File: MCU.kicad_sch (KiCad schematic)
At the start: 33 parts, among them J7 RS485, J8 JTAG, J9 USB-C, SW1 SYS_RESET, SW2 BOOT0, U10 LTC2851xS8, U11 USBLC6-2SC6, U9 STM32G474MBTx, Y1 16MHz

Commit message: reorg and add 10MHz
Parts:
- removed TP7: VBUS, TestPoint:TestPoint_Keystone_5015_Micro_Mini, symbol Connector:TestPoint_Small
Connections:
- net +3.3V: now also U10.1 (VCC)
- net GND: now also U10.4 (GND)
- net VBUS: now reaches J9.A4 (VBUS), J9.A9 (VBUS), J9.B4 (VBUS), J9.B9 (VBUS)
- net EN_RF4: now reaches U9.36 (PE13)
- net PG_RF4: now reaches U9.37 (PE14)
- net BUCK_VIN renamed BUCKIN_SENSE
- net BUCK_VOUT renamed BUCKOUT_SENSE
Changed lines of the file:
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@@
 	(wire
 		(pts
+			(xy 176.53 92.71) (xy 176.53 99.06)
+		)
+		(stroke
+			(width 0)
+			(type default)
+		)
+	)
+	(wire
+		(pts
 			(xy 69.85 146.05) (xy 72.39 146.05)
 		)
@@
 	(wire
 		(pts
-			(xy 114.3 41.91) (xy 124.46 41.91)
+			(xy 114.3 41.91) (xy 130.81 41.91)
 		)
 		(stroke
@@
 	(wire
 		(pts
+			(xy 121.92 44.45) (xy 130.81 44.45)
+		)
+		(stroke
+			(width 0)
+			(type default)
+		)
+	)
+	(wire
+		(pts
 			(xy 114.3 24.13) (xy 121.92 24.13)
 		)
@@
 	(wire
 		(pts
+			(xy 44.45 69.85) (xy 49.53 69.85)
+		)
+		(stroke
+			(width 0)
+			(type default)
+		)
+	)
+	(wire
+		(pts
 			(xy 44.45 125.73) (xy 49.53 125.73)
 		)
@@
 	(wire
 		(pts
-			(xy 99.06 36.83) (xy 124.46 36.83)
+			(xy 99.06 36.83) (xy 130.81 36.83)
 		)
 		(stroke
@@
 	(wire
 		(pts
-			(xy 121.92 31.75) (xy 121.92 44.45)
-		)
-		(stroke
-			(width 0)
-			(type default)
-		)
-	)
-	(wire
-		(pts
 			(xy 34.29 44.45) (xy 44.45 44.45)
 		)
@@
 	(wire
 		(pts
+			(xy 176.53 54.61) (xy 176.53 62.23)
+		)
+		(stroke
+			(width 0)
+			(type default)
+		)
+	)
+	(wire
+		(pts
 			(xy 44.45 41.91) (xy 49.53 41.91)
 		)
@@
 	(wire
 		(pts
-			(xy 121.92 44.45) (xy 124.46 44.45)
+			(xy 234.95 113.03) (xy 234.95 115.57)
 		)
 		(stroke
@@
 	(wire
 		(pts
+			(xy 121.92 31.75) (xy 121.92 44.45)
+		)
+		(stroke
+			(width 0)
+			(type default)
+		)
+	)
+	(wire
+		(pts
 			(xy 214.63 92.71) (xy 214.63 95.25)
 		)
@@
 	(wire
 		(pts
+			(xy 44.45 72.39) (xy 49.53 72.39)
+		)
+		(stroke
+			(width 0)
+			(type default)
+		)
+	)
+	(wire
+		(pts
 			(xy 22.86 17.78) (xy 22.86 20.32)
 		)
@@
 	(wire
 		(pts
-			(xy 106.68 39.37) (xy 124.46 39.37)
+			(xy 106.68 39.37) (xy 130.81 39.37)
 		)
 		(stroke
@@
 		)
 	)
-	(hierarchical_label "BUCK_VOUT"
+	(hierarchical_label "BUCKOUT_SENSE"
 		(shape input)
-		(at 124.46 44.45 0)
+		(at 130.81 44.45 0)
 		(effects
 			(font
@@
 	(hierarchical_label "RFVA"
 		(shape input)
-		(at 124.46 36.83 0)
+		(at 130.81 36.83 0)
 		(effects
 			(font
@@
 		)
 	)
+	(hierarchical_label "EN_RF4"
+		(shape input)
+		(at 44.45 69.85 180)
+		(effects
+			(font
+				(size 1.27 1.27)
+			)
+			(justify right)
+		)
+	)
 	(hierarchical_label "RF_ISENSE"
 		(shape input)
@@
 		)
 	)
-	(hierarchical_label "BUCK_VIN"
+	(hierarchical_label "BUCKIN_SENSE"
 		(shape input)
-		(at 124.46 39.37 0)
+		(at 130.81 39.37 0)
 		(effects
 			(font
@@
 	(hierarchical_label "RFVB"
 		(shape input)
-		(at 124.46 41.91 0)
+		(at 130.81 41.91 0)
 		(effects
 			(font
@@
 		)
 	)
-	(hierarchical_label "SOC_ISENSE"
+	(hierarchical_label "PG_RF4"
 		(shape input)
-		(at 44.45 97.79 180)
+		(at 44.45 72.39 180)
 		(effects
 			(font
@@
 		)
 	)
-	(symbol
-		(lib_id "Connector:TestPoint_Small")
-		(at 234.95 115.57 0)
-		(mirror y)
-		(unit 1)
-		(exclude_from_sim no)
-		(in_bom yes)
-		(on_board yes)
-		(dnp no)
-		(property "Reference" "TP7"
-			(at 236.22 114.2999 0)
-			(effects
-				(font
-					(size 1.27 1.27)
-				)
-				(justify right)
-			)
-		)
-		(property "Value" "VBUS"
-			(at 236.22 116.8399 0)
-			(effects
-				(font
-					(size 1.27 1.27)
-				)
-				(justify right)
-			)
-		)
-		(property "Footprint" "TestPoint:TestPoint_Keystone_5015_Micro_Mini"
-			(at 229.87 115.57 0)
-			(effects
-				(font
-					(size 1.27 1.27)
-				)
-				(hide yes)
-			)
-		)
-		(property "Datasheet" "~"
-			(at 229.87 115.57 0)
-			(effects
-				(font
-					(size 1.27 1.27)
-				)
-				(hide yes)
-			)
-		)
-		(property "Description" "test point"
-			(at 234.95 115.57 0)
-			(effects
-				(font
-					(size 1.27 1.27)
-				)
-				(hide yes)
-			)
-		)
-		(property "DIGIKEY_PN" "36-5015CT-ND"
-			(at 234.95 115.57 0)
-			(effects
-				(font
-					(size 1.27 1.27)
-				)
-				(hide yes)
-			)
-		)
-		(pin "1"
-		)
-		(instances
-			(project "huskypointofload"
-				(path "/eb9c972b-d134-41da-be97-ece3f463f7e0/aad3f0e3-dcbe-4112-94dc-37caa60c9eb1"
-					(reference "TP7")
-					(unit 1)
-				)
+	(hierarchical_label "SOC_ISENSE"
+		(shape input)
+		(at 44.45 97.79 180)
+		(effects
+			(font
+				(size 1.27 1.27)
 			)
+			(justify right)
 		)
 	)
@@
 	)
 	(symbol
+		(lib_id "power:VBUS")
+		(at 234.95 113.03 0)
+		(unit 1)
+		(exclude_from_sim no)
+		(in_bom yes)
+		(on_board yes)
+		(dnp no)
+		(fields_autoplaced yes)
+		(property "Reference" "#PWR072"
+			(at 234.95 116.84 0)
+			(effects
+				(font
+					(size 1.27 1.27)
+				)
+				(hide yes)
+			)
+		)
+		(property "Value" "VBUS"
+			(at 234.95 107.95 0)
+			(effects
+				(font
+					(size 1.27 1.27)
+				)
+			)
+		)
+		(property "Footprint" ""
+			(at 234.95 113.03 0)
+			(effects
+				(font
+					(size 1.27 1.27)
+				)
+				(hide yes)
+			)
+		)
+		(property "Datasheet" ""
+			(at 234.95 113.03 0)
+			(effects
+				(font
+					(size 1.27 1.27)
+				)
+				(hide yes)
+			)
+		)
+		(property "Description" "Power symbol creates a global label with name \"VBUS\""
+			(at 234.95 113.03 0)
+			(effects
+				(font
+					(size 1.27 1.27)
+				)
+				(hide yes)
+			)
+		)
+		(pin "1"
+		)
+		(instances
+			(project ""
+				(path "/eb9c972b-d134-41da-be97-ece3f463f7e0/aad3f0e3-dcbe-4112-94dc-37caa60c9eb1"
+					(reference "#PWR072")
+					(unit 1)
+				)
+			)
+		)
+	)
+	(symbol
 		(lib_id "power:GND")
 		(at 22.86 30.48 0)
@@
 	)
 	(symbol
+		(lib_id "power:+3.3V")
+		(at 176.53 54.61 0)
+		(unit 1)
+		(exclude_from_sim no)
+		(in_bom yes)
+		(on_board yes)
+		(dnp no)
+		(fields_autoplaced yes)
+		(property "Reference" "#PWR0103"
+			(at 176.53 58.42 0)
+			(effects
+				(font
+					(size 1.27 1.27)
+				)
+				(hide yes)
+			)
+		)
+		(property "Value" "+3.3V"
+			(at 176.53 49.53 0)
+			(effects
+				(font
+					(size 1.27 1.27)
+				)
+			)
+		)
+		(property "Footprint" ""
+			(at 176.53 54.61 0)
+			(effects
+				(font
+					(size 1.27 1.27)
+				)
+				(hide yes)
+			)
+		)
+		(property "Datasheet" ""
+			(at 176.53 54.61 0)
+			(effects
+				(font
+					(size 1.27 1.27)
+				)
+				(hide yes)
+			)
+		)
+		(property "Description" "Power symbol creates a global label with name \"+3.3V\""
+			(at 176.53 54.61 0)
+			(effects
+				(font
+					(size 1.27 1.27)
+				)
+				(hide yes)
+			)
+		)
+		(pin "1"
+		)
+		(instances
+			(project "huskypointofload"
+				(path "/eb9c972b-d134-41da-be97-ece3f463f7e0/aad3f0e3-dcbe-4112-94dc-37caa60c9eb1"
+					(reference "#PWR0103")
+					(unit 1)
+				)
+			)
+		)
+	)
+	(symbol
 		(lib_id "Device:C_Small")
 		(at 217.17 31.75 0)
@@
 					(unit 1)
 				)
+			)
+		)
+	)
+	(symbol
+		(lib_id "power:GND")
+		(at 176.53 99.06 0)
+		(unit 1)
+		(exclude_from_sim no)
+		(in_bom yes)
+		(on_board yes)
+		(dnp no)
+		(fields_autoplaced yes)
+		(property "Reference" "#PWR0100"
+			(at 176.53 105.41 0)
+			(effects
+				(font
+					(size 1.27 1.27)
+				)
+				(hide yes)
+			)
+		)
+		(property "Value" "GND"
+			(at 176.53 104.14 0)
+			(effects
+				(font
+					(size 1.27 1.27)
+				)
+			)
+		)
+		(property "Footprint" ""
+			(at 176.53 99.06 0)
+			(effects
+				(font
+					(size 1.27 1.27)
+				)
+				(hide yes)
+			)
+		)
+		(property "Datasheet" ""
+			(at 176.53 99.06 0)
+			(effects
+				(font
+					(size 1.27 1.27)
+				)
+				(hide yes)
+			)
+		)
+		(property "Description" "Power symbol creates a global label with name \"GND\" , ground"
+			(at 176.53 99.06 0)
+			(effects
+				(font
+					(size 1.27 1.27)
+				)
+				(hide yes)
+			)
+		)
+		(pin "1"
+		)
+		(instances
+			(project "huskypointofload"
+				(path "/eb9c972b-d134-41da-be97-ece3f463f7e0/aad3f0e3-dcbe-4112-94dc-37caa60c9eb1"
+					(reference "#PWR0100")
+					(unit 1)
+				)

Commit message: Renumber refdes
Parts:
- renumbered C75 to C69, C76 to C70, C77 to C71, C78 to C72, C79 to C73, C80 to C74, C81 to C75, C82 to C76, C83 to C77, C84 to C78, C85 to C79, C86 to C80, J7 to J6, J8 to J7, J9 to J8, R39 to R27, R40 to R28, R41 to R29, R42 to R30, R43 to R31, R44 to R32, TP8 to TP7, U9 to U7, U10 to U8, U11 to U9

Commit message: Add LMX Draft
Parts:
- added R30, R34: 4.7k, Resistor_SMD:R_0402_1005Metric, symbol Device:R_Small
- renumbered R30 to R31, R31 to R32, R32 to R33
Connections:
- net BOOT_RX: now also U7.67 (PC11); no longer U7.66 (PC10)
- net BOOT_TX: now also U7.66 (PC10); no longer U7.67 (PC11)
- net D+: now also U9.4 (I/O2); no longer U9.3 (I/O2)
- net D-: now also U9.6 (I/O1); no longer U9.1 (I/O1)
- net DESD+: now also U9.3 (I/O2); no longer U9.4 (I/O2)
- net DESD-: now also U9.1 (I/O1); no longer U9.6 (I/O1)
- net GND: now also R30.2, R34.2
- net TDO: now also U7.72 (PB3); no longer U7.73 (PB4)
- net CC1: now reaches J8.A5 (CC1)
- net CC1: now also R30.1
- net CC2: now reaches J8.B5 (CC2)
- net CC2: now also R34.1
- no-connect marks 2 -> 0
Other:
- moved on the sheet: R32, R33, U9

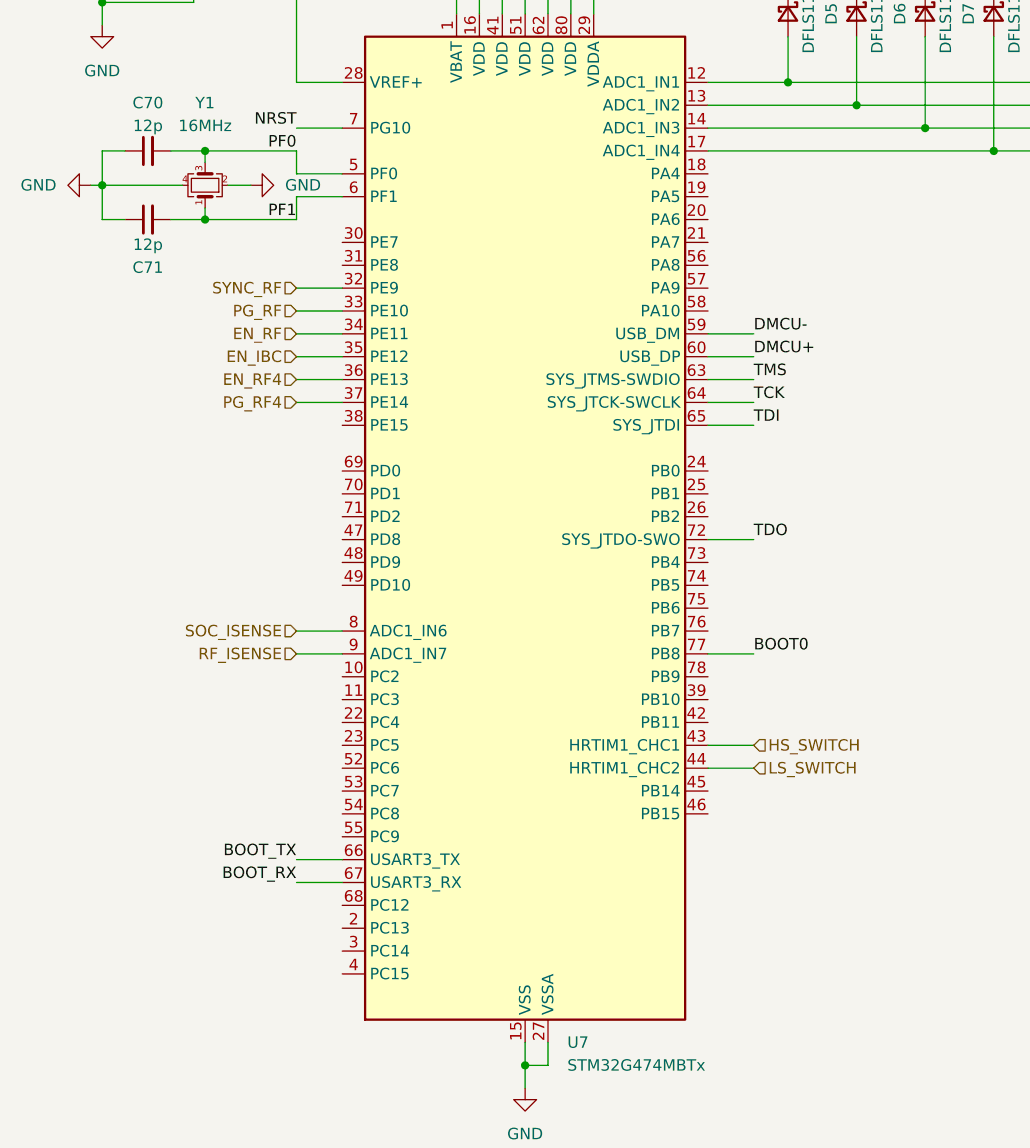
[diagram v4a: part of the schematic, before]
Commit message: Different Matching Circuit
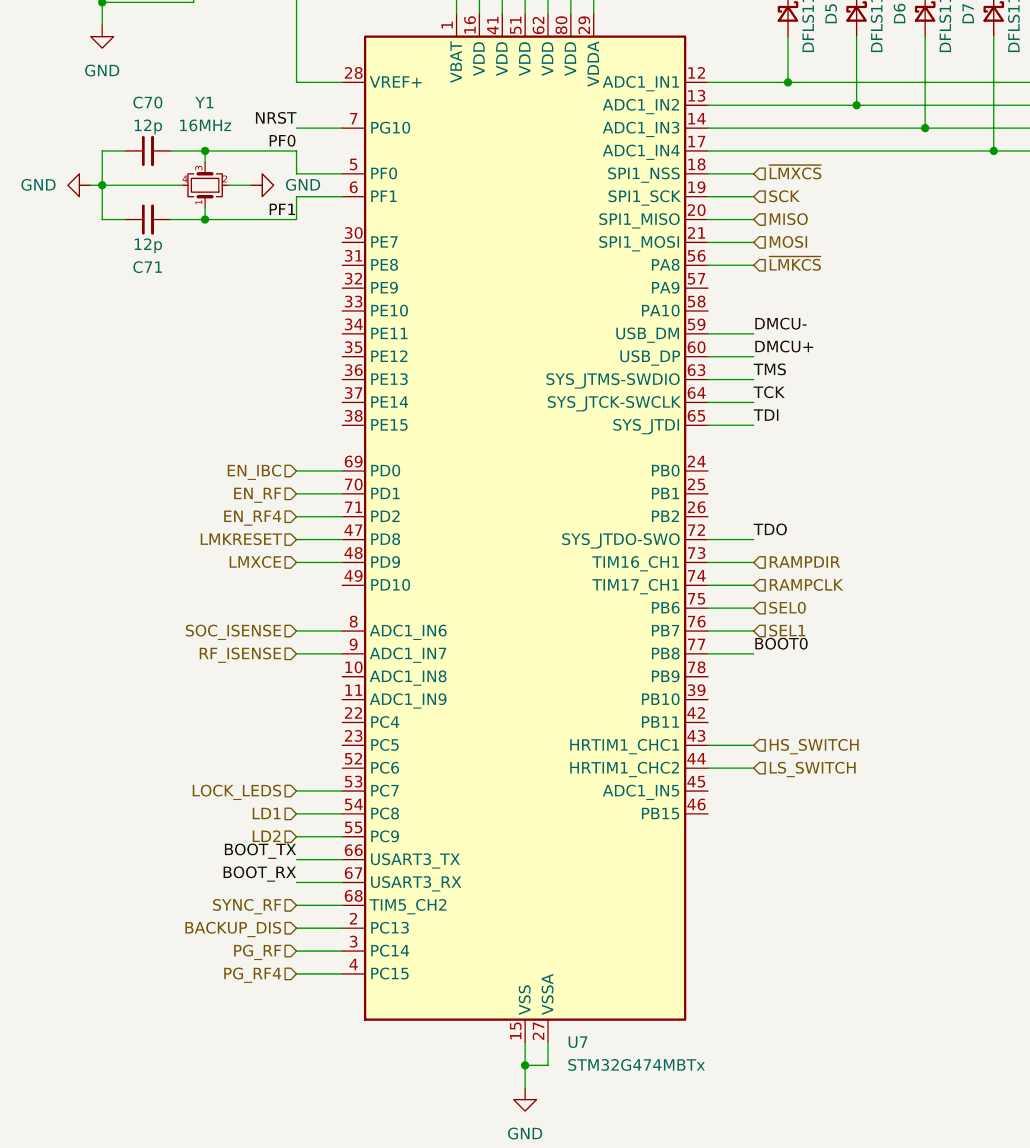
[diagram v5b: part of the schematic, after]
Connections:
- net EN_IBC: now also U7.69 (PD0); no longer U7.35 (PE12)
- net EN_RF: now also U7.70 (PD1); no longer U7.34 (PE11)
- net EN_RF4: now also U7.71 (PD2); no longer U7.36 (PE13)
- net PG_RF: now also U7.3 (PC14); no longer U7.33 (PE10)
- net PG_RF4: now also U7.4 (PC15); no longer U7.37 (PE14)
- net SYNC_RF: now also U7.68 (PC12); no longer U7.32 (PE9)
- net ~{LMXCS}: now reaches U7.18 (PA4)
- net SCK: now reaches U7.19 (PA5)
- net BACKUP_DIS: now reaches U7.2 (PC13)
- net MISO: now reaches U7.20 (PA6)
- net MOSI: now reaches U7.21 (PA7)
- net LMKRESET: now reaches U7.47 (PD8)
- net LMXCE: now reaches U7.48 (PD9)
- net LOCK_LEDS: now reaches U7.53 (PC7)
- net LD1: now reaches U7.54 (PC8)
- net LD2: now reaches U7.55 (PC9)
- net ~{LMKCS}: now reaches U7.56 (PA8)
- net RAMPDIR: now reaches U7.73 (PB4)
- net RAMPCLK: now reaches U7.74 (PB5)
- net SEL0: now reaches U7.75 (PB6)
- net SEL1: now reaches U7.76 (PB7)
